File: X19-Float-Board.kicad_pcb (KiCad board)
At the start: 2 copper layers, 100 x 100 mm, 26 parts, among them J1 Motor, J2 Conn_01x04_Pin, J3 Screw_Terminal_01x02, Q1 NMOS, SW2 SW_Nidec_CAS-120A1, U2 LM2596S-3.3, U3 STM32G431RBT6

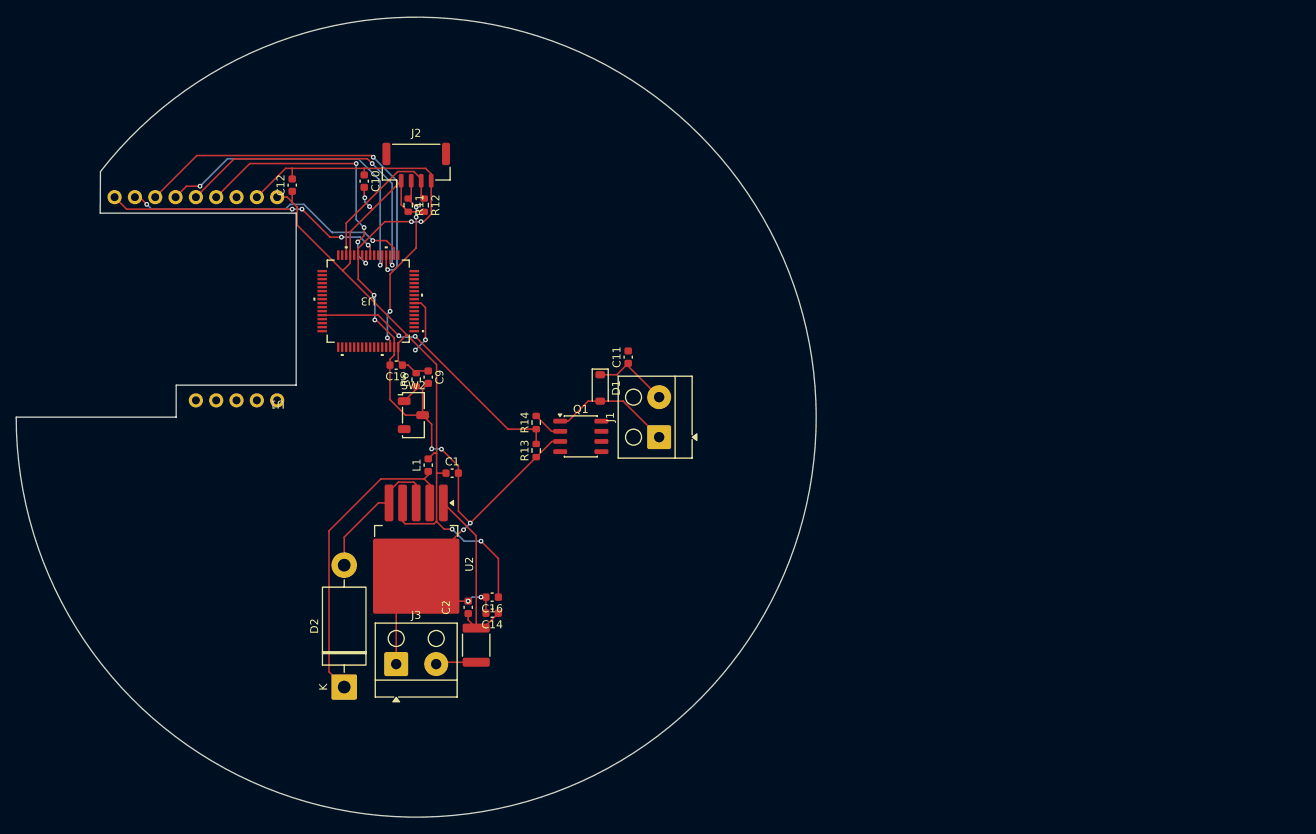
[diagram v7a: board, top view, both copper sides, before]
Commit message: USB-C + Complete wiring
Compltetly wired the pcb (I don't understand the DRC errors) and added a usb C to flash the stm, modified the switch to be the BOOT0 for the stm so it controls whether the stm is in flash mode
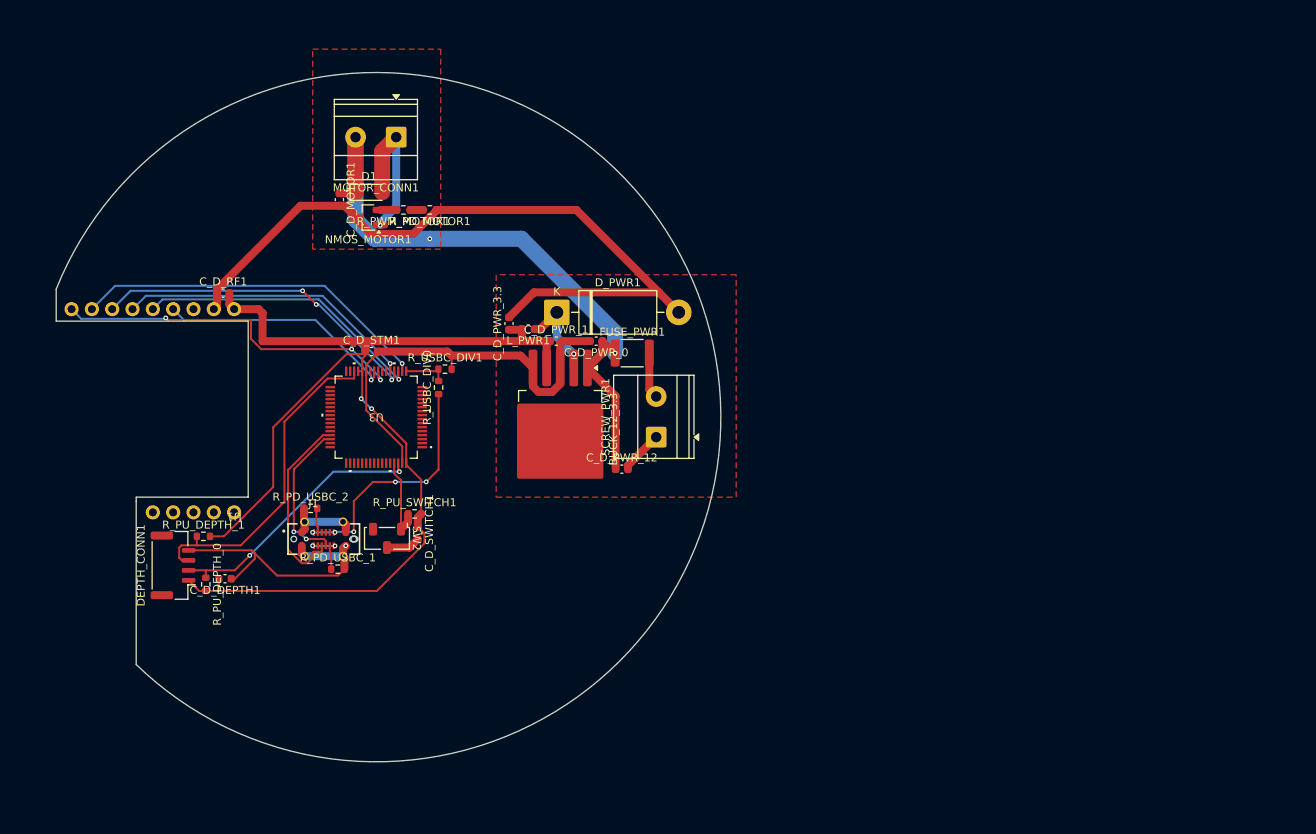
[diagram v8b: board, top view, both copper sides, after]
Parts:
- removed C1: 220µF, Capacitor_SMD:C_0603_1608Metric
- removed C10, C11, C12, C13, C9: 100nF, Capacitor_SMD:C_0603_1608Metric
- removed C14, C16: 4.7µF, Capacitor_SMD:C_0603_1608Metric
- removed C2: 680µF, Capacitor_SMD:C_0603_1608Metric
- removed D2: 1N5822, Diode_THT:D_DO-201AD_P15.24mm_Horizontal
- removed F1: 2A 12V PTC fuse, Fuse:Fuse_1812_4532Metric
- removed J2: Conn_01x04_Pin, Connector_JST:JST_GH_BM04B-GHS-TBT_1x04-1MP_P1.25mm_Vertical
- removed J3: Screw_Terminal_01x02, TerminalBlock_Altech:Altech_AK100_1x02_P5.00mm
- removed L1: 33µH, Inductor_SMD:L_0603_1608Metric
- removed Q1: NMOS, Package_SO:SO-8_3.9x4.9mm_P1.27mm
- removed R11, R12: 4.7kΩ, Resistor_SMD:R_0603_1608Metric
- removed R13, R6: 10kΩ, Resistor_SMD:R_0603_1608Metric
- removed R14: 220Ω, Resistor_SMD:R_0603_1608Metric
- removed U2: LM2596S-3.3, Package_TO_SOT_SMD:TO-263-5_TabPin3
- added BUCK_12_3.3: LM2596S-3.3, Package_TO_SOT_SMD:TO-263-5_TabPin3, F.Cu at (168.0, 101.5)
- added C_D_DEPTH1: 100nF, Capacitor_SMD:C_0603_1608Metric, F.Cu at (126.1, 120.2)
- added C_D_MOTOR1: 100nF, Capacitor_SMD:C_0603_1608Metric, F.Cu at (140.4, 72.8)
- added C_D_PWR_0: 680µF, Capacitor_SMD:C_0603_1608Metric, F.Cu at (172.5, 90.5)
- added C_D_PWR_1: 220µF, Capacitor_SMD:C_0603_1608Metric, F.Cu at (167.5, 90.5)
- added C_D_PWR_12: 4.7µF, Capacitor_SMD:C_0603_1608Metric, F.Cu at (175.7, 106.5)
- added C_D_PWR_3.3: 4.7µF, Capacitor_SMD:C_0603_1608Metric, F.Cu at (161.6, 88.3)
- added C_D_RF1: 100nF, Capacitor_SMD:C_0603_1608Metric, F.Cu at (125.9, 84.5)
- added C_D_STM1: 100nF, Capacitor_SMD:C_0603_1608Metric, F.Cu at (144.4, 91.8)
- added C_D_SWITCH1: 100nF, Capacitor_SMD:C_0603_1608Metric, F.Cu at (150.2, 114.5)
- added DEPTH_CONN1: Conn_01x04_Pin, Connector_JST:JST_GH_BM04B-GHS-TBT_1x04-1MP_P1.25mm_Vertical, F.Cu at (119.6, 118.5)
- added D_PWR1: 1N5822, Diode_THT:D_DO-201AD_P15.24mm_Horizontal, F.Cu at (167.6, 86.9)
- added FUSE_PWR1: 2A 12V PTC fuse, Fuse:Fuse_1812_4532Metric, F.Cu at (177.0, 92.0)
- added L_PWR1: 33µH, Inductor_SMD:L_0603_1608Metric, F.Cu at (164.0, 89.0)
- added MOTOR_CONN1: Motor, TerminalBlock_Phoenix:TerminalBlock_Phoenix_MKDS-1,5-2-5.08_1x02_P5.08mm_Horizontal, F.Cu at (147.5, 65.0)
- added NMOS_MOTOR1: NMOS, Package_TO_SOT_SMD:SOT-23_Handsoldering, F.Cu at (144.0, 75.0)
- added R_PD_MOTOR1: 10kΩ, Resistor_SMD:R_0603_1608Metric, F.Cu at (151.7, 74.1)
- added R_PD_USBC_1: 5.1k, Resistor_SMD:R_0603_1608Metric, F.Cu at (140.2, 119.0)
- added R_PD_USBC_2: 5.1kΩ, Resistor_SMD:R_0603_1608Metric, F.Cu at (136.8, 111.4)
- added R_PU_DEPTH_0: 4.7kΩ, Resistor_SMD:R_0603_1608Metric, F.Cu at (123.7, 120.9)
- added R_PU_DEPTH_1: 4.7kΩ, Resistor_SMD:R_0603_1608Metric, F.Cu at (123.4, 114.9)
- added R_PU_SWITCH1: 10kΩ, Resistor_SMD:R_0603_1608Metric, F.Cu at (149.8, 112.1)
- added R_PWM_MOTOR1: 220Ω, Resistor_SMD:R_0603_1608Metric, F.Cu at (148.4, 74.1)
- added R_USBC_DIV0: 20kΩ, Resistor_SMD:R_0603_1608Metric, F.Cu at (152.8, 96.3)
- added R_USBC_DIV1: 10kΩ, Resistor_SMD:R_0603_1608Metric, F.Cu at (153.6, 94.0)
- added SCREW_PWR1: Screw_Terminal_01x02, TerminalBlock_Phoenix:TerminalBlock_Phoenix_MKDS-1,5-2-5.08_1x02_P5.08mm_Horizontal, F.Cu at (180.0, 102.5)
- D1: value D_Schottky -> D_MOTOR
- J1: value Motor -> USB4220-03-1040-C_REVA; footprint TerminalBlock_Altech:Altech_AK100_1x02_P5.00mm -> usbc:GCT_USB4220-03-1040-C_REVA
- moved J1 43.8 mm to (138.4, 115.2), turned to 0 degrees
- moved D1 37.9 mm to (144.1, 71.9), turned to 0 degrees
- moved SW2 15.7 mm to (146.3, 115.2), turned to -90 degrees
- moved U1 15.0 mm to (127.2, 111.9)
- moved U3 14.5 mm to (145.0, 100.0)
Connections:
- D1 pad 1: 12V -> 12 V
- U3 pad 17: unconnected-(U3A-PA3-Pad17) -> Net-(U3A-PA3)
- U3 pad 28: 3.3V -> 3.3 V
- U3 pad 45: unconnected-(U3A-PA11-Pad45) -> Net-(J1-DN2)
- U3 pad 46: unconnected-(U3A-PA12-Pad46) -> Net-(J1-DP2)
- U3 pad 61: unconnected-(U3A-PB8-BOOT0-Pad61) -> /Switch/switch
- U3 pad 8: /Switch/switch -> unconnected-(U3A-PC0-Pad8)
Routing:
- net 12 V: track 23.1 -> 80.6 mm, vias 0 -> 2
- net 3.3 V: track 106.6 -> 149.3 mm, vias 4 -> 3
- net Net-(D2-K): track 39.3 -> 0.00 mm
- net GND: track 162.5 -> 200.7 mm, vias 10 -> 4
- net /Motor/Motor PWM: track 34.6 -> 1.65 mm, vias 2 -> 0
- net VBUS_A: track 0.00 -> 31.0 mm, vias 0 -> 5
- net Net-(J1-DN2): track 0.00 -> 23.7 mm
- net /sensor/Depth SDA: track 19.0 -> 41.1 mm
- net Net-(J1-DP2): track 0.00 -> 19.0 mm, vias 0 -> 2
- net Net-(BUCK_12_3.3-OUT): track 0.00 -> 11.5 mm, vias 0 -> 2
- net /sensor/Depth SCL: track 23.0 -> 33.5 mm, vias 4 -> 2
- net 12V: track 9.92 -> 0.00 mm
- net /rf/RF RST: track 35.5 -> 45.4 mm, vias 4 -> 3
- net /rf/RF NSS: track 36.4 -> 45.0 mm, vias 2 -> 1
- net Net-(SCREW_PWR1-Pin_2): track 0.00 -> 5.78 mm
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- added copper zone on F.Cu, net 12 V
- added copper zone on F.Cu, net GND
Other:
- board size 100 x 100 mm -> 83.1 x 86.2 mm
